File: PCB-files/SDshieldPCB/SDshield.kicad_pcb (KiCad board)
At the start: 2 copper layers, 35.8 x 18.2 mm, 9 parts, among them J1 SD-Karte 9-pin push-push, J2 SCK, J3 MOSI/MISO, J4 GND/VCC, J5 GND|CS, U1 74LVTH125PW,118

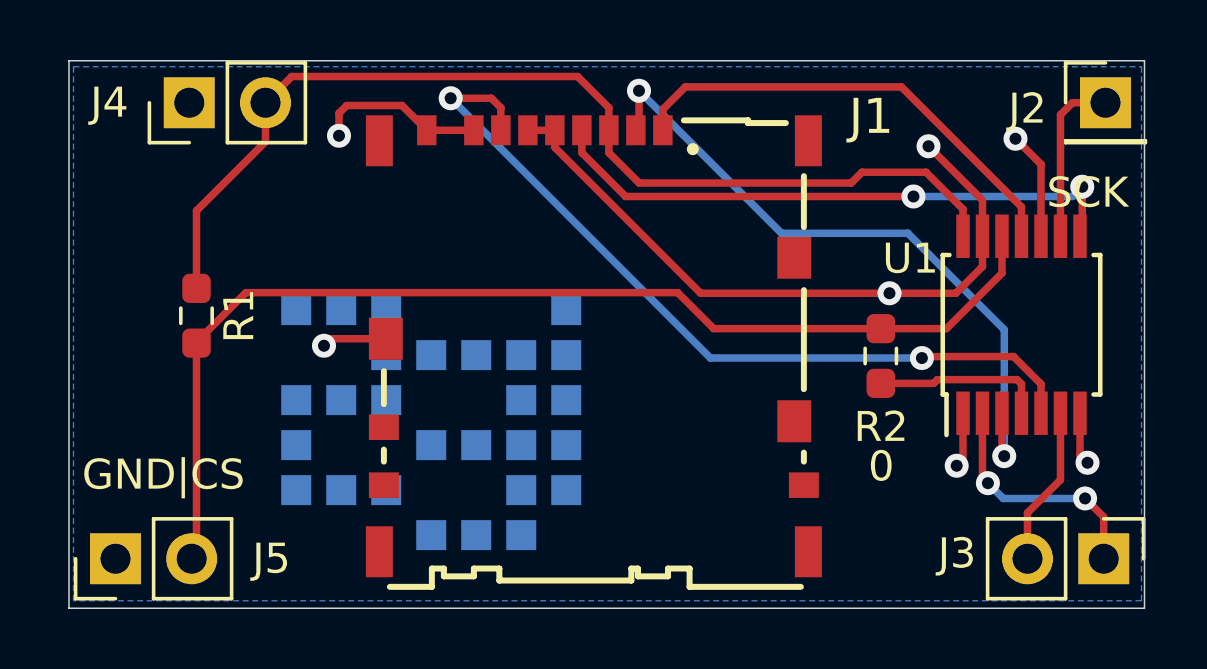
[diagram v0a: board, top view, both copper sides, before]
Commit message: New SD Card PCB
In Altium designer, to use würth elektroniks lib
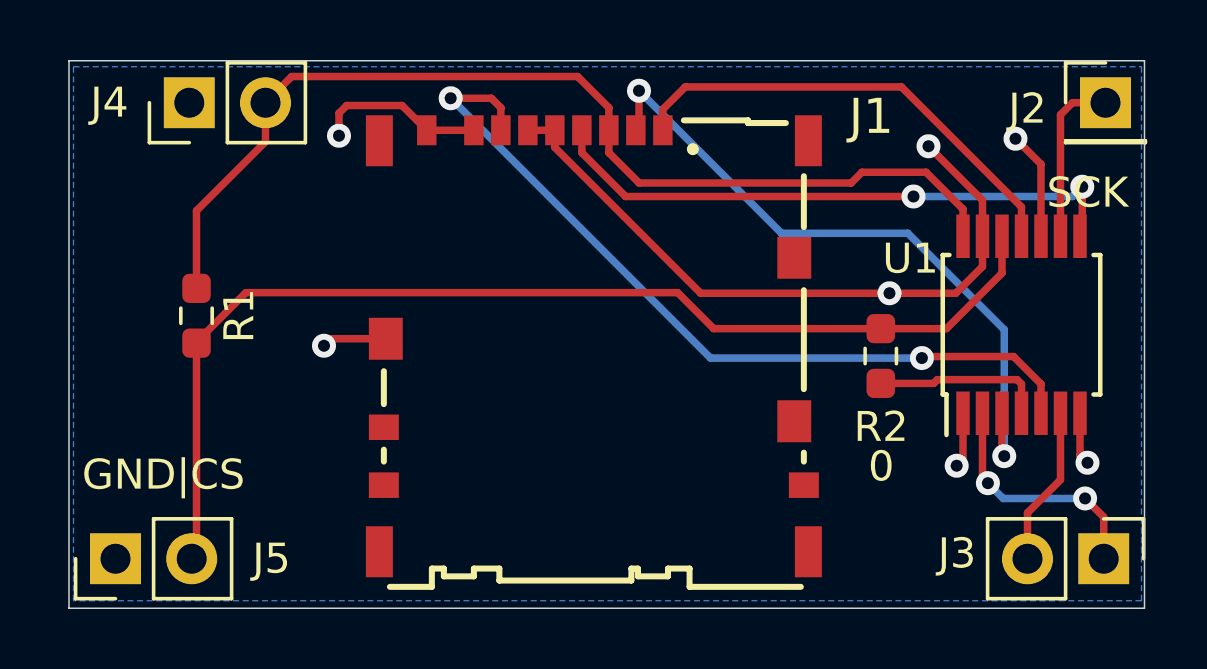
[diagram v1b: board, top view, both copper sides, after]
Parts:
- removed REF**: IES_Logo, IES_Logo:IES_Logo
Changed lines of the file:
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@@
     )
-  )
-  (footprint "IES_Logo:IES_Logo" (layer "B.Cu")
-    (at 146.325 85.8125 180)
-    (attr smd)
-    (fp_text reference "REF**" (at 4.15 1.42 unlocked) (layer "B.SilkS") hide
-      (effects (font (size 1 1) (thickness 0.15)) (justify mirror))
-    )
-    (fp_text value "IES_Logo" (at 4.15 -0.08 unlocked) (layer "B.Fab")
-      (effects (font (size 1 1) (thickness 0.15)) (justify mirror))
-    )
-    (fp_rect (start 3 -9.5) (end 4 -10.5) (layer "B.SilkS") (width 0.05) (fill none))
-    (fp_rect (start 4.5 -6.5) (end 5.5 -7.5) (layer "B.SilkS") (width 0.05) (fill none))
-    (fp_rect (start 0 -5) (end 1 -6) (layer "B.SilkS") (width 0.05) (fill none))
-    (fp_rect (start 4.5 -9.5) (end 5.5 -10.5) (layer "B.SilkS") (width 0.05) (fill none))
-    (fp_rect (start 1.5 -8) (end 2.5 -9) (layer "B.SilkS") (width 0.05) (fill none))
-    (fp_rect (start -1.5 -2) (end -0.5 -3) (layer "B.SilkS") (width 0.05) (fill none))
-    (fp_rect (start 4.5 -3.5) (end 5.5 -4.5) (layer "B.SilkS") (width 0.05) (fill none))
-    (fp_rect (start -3 -9.5) (end -2 -10.5) (layer "B.SilkS") (width 0.05) (fill none))
-    (fp_rect (start 6 -9.5) (end 7 -10.5) (layer "B.SilkS") (width 0.05) (fill none))
-    (fp_rect (start 6 -3.5) (end 7 -4.5) (layer "B.SilkS") (width 0.05) (fill none))
-    (fp_rect (start 3 -6.5) (end 4 -7.5) (layer "B.SilkS") (width 0.05) (fill none))
-    (fp_rect (start 0 -2) (end 1 -3) (layer "B.SilkS") (width 0.05) (fill none))
-    (fp_rect (start 0 -8) (end 1 -9) (layer "B.SilkS") (width 0.05) (fill none))
-    (fp_rect (start 1.5 -5) (end 2.5 -6) (layer "B.SilkS") (width 0.05) (fill none))
-    (fp_rect (start 1.5 -2) (end 2.5 -3) (layer "B.SilkS") (width 0.05) (fill none))
-    (pad "1" smd rect (at -2.5 -2.5 180) (size 1 1) (layers "B.Cu" "B.Paste" "B.Mask"))
-    (pad "5" smd rect (at 3.5 -2.5 180) (size 1 1) (layers "B.Cu" "B.Paste" "B.Mask"))
-    (pad "6" smd rect (at 5 -2.5 180) (size 1 1) (layers "B.Cu" "B.Paste" "B.Mask"))
-    (pad "7" smd rect (at 6.5 -2.5 180) (size 1 1) (layers "B.Cu" "B.Paste" "B.Mask"))
-    (pad "8" smd rect (at -2.5 -4 180) (size 1 1) (layers "B.Cu" "B.Paste" "B.Mask"))
-    (pad "9" smd rect (at -1 -4 180) (size 1 1) (layers "B.Cu" "B.Paste" "B.Mask"))
-    (pad "10" smd rect (at 0.5 -4 180) (size 1 1) (layers "B.Cu" "B.Paste" "B.Mask"))
-    (pad "11" smd rect (at 2 -4 180) (size 1 1) (layers "B.Cu" "B.Paste" "B.Mask"))
-    (pad "12" smd rect (at 3.5 -4 180) (size 1 1) (layers "B.Cu" "B.Paste" "B.Mask"))
-    (pad "15" smd rect (at -2.5 -5.5 180) (size 1 1) (layers "B.Cu" "B.Paste" "B.Mask"))
-    (pad "16" smd rect (at -1 -5.5 180) (size 1 1) (layers "B.Cu" "B.Paste" "B.Mask"))
-    (pad "19" smd rect (at 3.5 -5.5 180) (size 1 1) (layers "B.Cu" "B.Paste" "B.Mask"))
-    (pad "20" smd rect (at 5 -5.5 180) (size 1 1) (layers "B.Cu" "B.Paste" "B.Mask"))
-    (pad "21" smd rect (at 6.5 -5.5 180) (size 1 1) (layers "B.Cu" "B.Paste" "B.Mask"))
-    (pad "22" smd rect (at -2.5 -7 180) (size 1 1) (layers "B.Cu" "B.Paste" "B.Mask"))
-    (pad "23" smd rect (at -1 -7 180) (size 1 1) (layers "B.Cu" "B.Paste" "B.Mask"))
-    (pad "24" smd rect (at 0.5 -7 180) (size 1 1) (layers "B.Cu" "B.Paste" "B.Mask"))
-    (pad "25" smd rect (at 2 -7 180) (size 1 1) (layers "B.Cu" "B.Paste" "B.Mask"))
-    (pad "28" smd rect (at 6.5 -7 180) (size 1 1) (layers "B.Cu" "B.Paste" "B.Mask"))
-    (pad "29" smd rect (at -2.5 -8.5 180) (size 1 1) (layers "B.Cu" "B.Paste" "B.Mask"))
-    (pad "30" smd rect (at -1 -8.5 180) (size 1 1) (layers "B.Cu" "B.Paste" "B.Mask"))
-    (pad "33" smd rect (at 3.5 -8.5 180) (size 1 1) (layers "B.Cu" "B.Paste" "B.Mask"))
-    (pad "34" smd rect (at 5 -8.5 180) (size 1 1) (layers "B.Cu" "B.Paste" "B.Mask"))
-    (pad "35" smd rect (at 6.5 -8.5 180) (size 1 1) (layers "B.Cu" "B.Paste" "B.Mask"))
-    (pad "37" smd rect (at -1 -10 180) (size 1 1) (layers "B.Cu" "B.Paste" "B.Mask"))
-    (pad "38" smd rect (at 0.5 -10 180) (size 1 1) (layers "B.Cu" "B.Paste" "B.Mask"))
-    (pad "39" smd rect (at 2 -10 180) (size 1 1) (layers "B.Cu" "B.Paste" "B.Mask"))
   )
   (gr_line (start 132.25 98.25) (end 132.25 80) (layer "Edge.Cuts") (width 0.05))
